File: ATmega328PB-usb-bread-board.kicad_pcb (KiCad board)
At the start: 2 copper layers, 60 x 60 mm, 32 parts, among them J1 Conn_01x17, J2 Conn_01x17, J3 USB_B_Micro, J4 AVR-ISP-6, J5 Grove-I2C-connector, J6 Grove-I2C-connector, J7 Grove-I2C-connector, U1 ATmega328PB-MU, U2 CP2102N-A01-GQFN28, U3 LMV358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

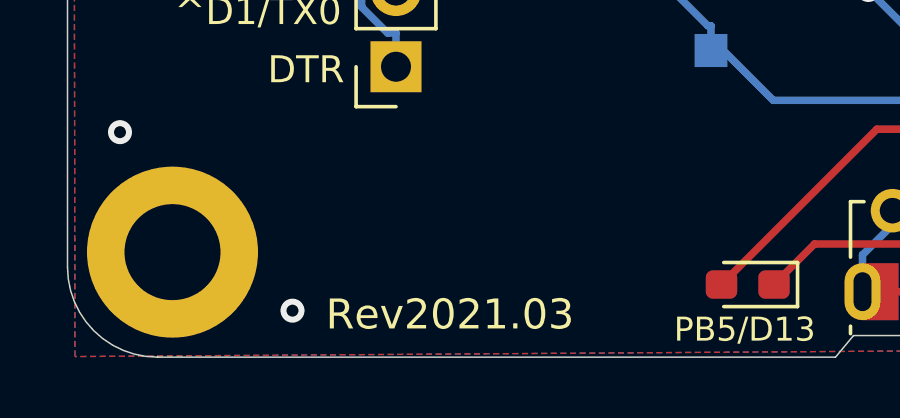
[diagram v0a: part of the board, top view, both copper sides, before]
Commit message: Update revision to Rev2021.04
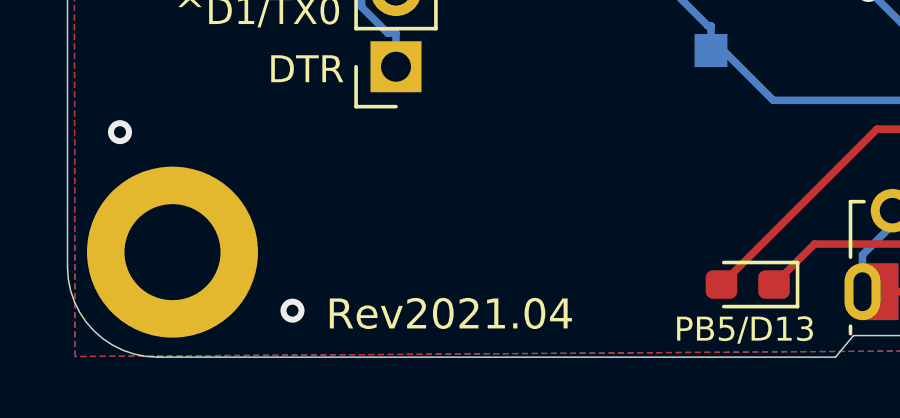
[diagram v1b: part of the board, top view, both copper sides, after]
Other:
- board text added: "Rev2021.04"
- board text removed: "Rev2021.03"
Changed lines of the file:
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@@
     (effects (font (size 1 1) (thickness 0.15)))
   )
-  (gr_text Rev2021.03 (at 112.75 108.58) (layer F.SilkS)
+  (gr_text Rev2021.04 (at 112.75 108.58) (layer F.SilkS)
     (effects (font (size 1 1) (thickness 0.15)))
   )

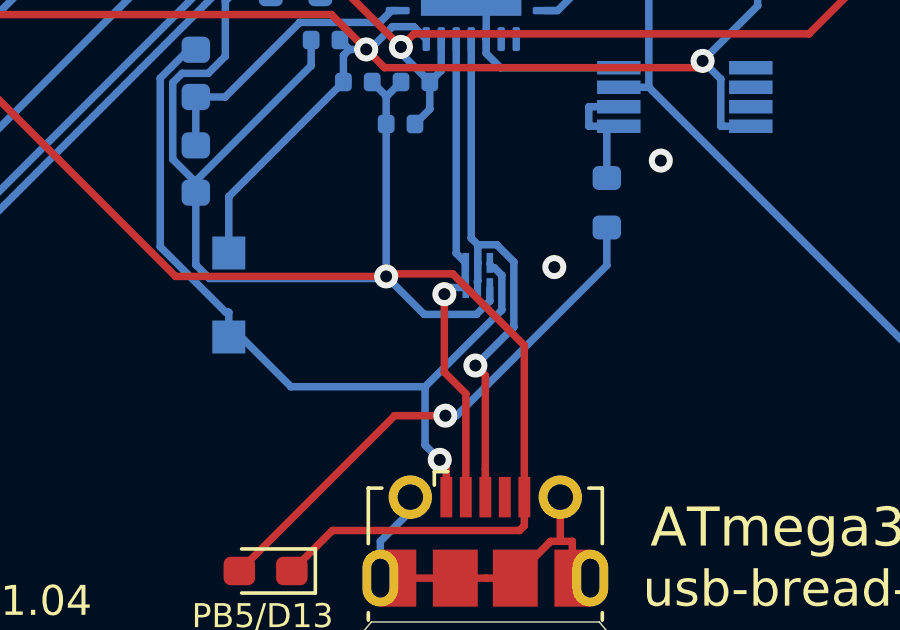
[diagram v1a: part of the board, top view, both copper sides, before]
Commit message: Expand pad for diode array
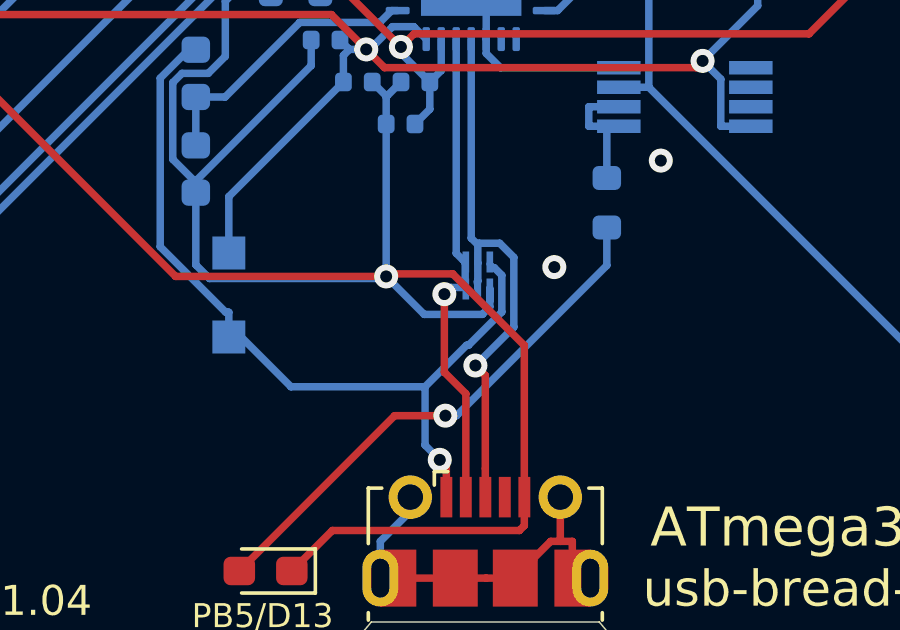
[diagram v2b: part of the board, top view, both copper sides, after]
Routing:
- net GND: track 252.6 -> 253.1 mm

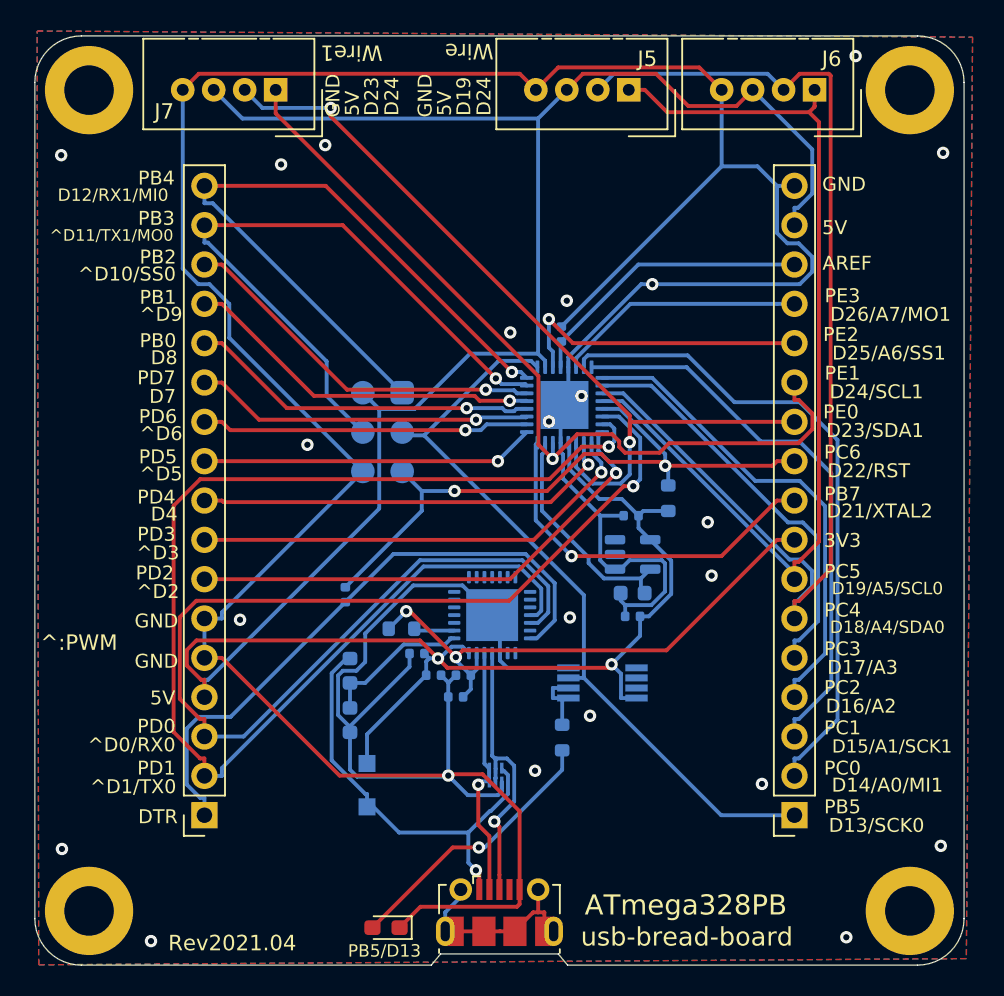
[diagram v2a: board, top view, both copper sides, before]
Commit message: Update footprint position of mems
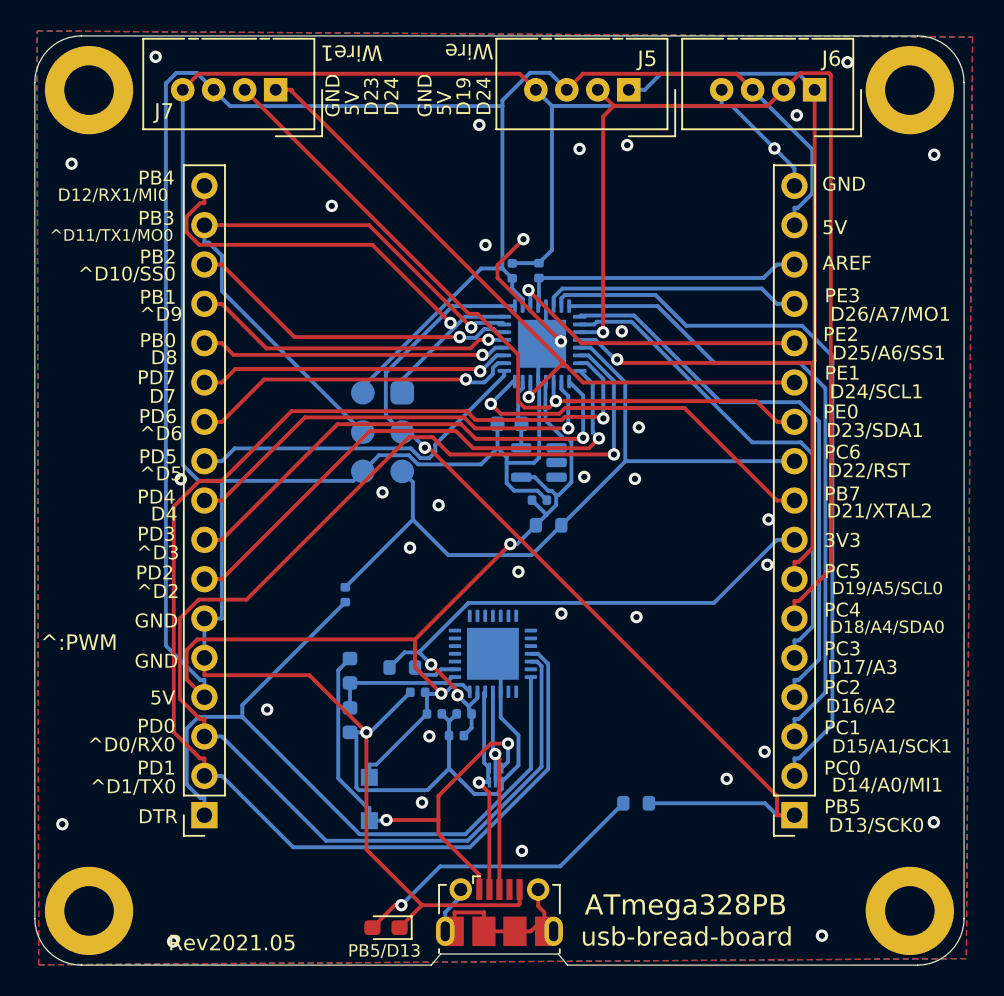
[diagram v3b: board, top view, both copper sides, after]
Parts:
- removed U3: LMV358, Package_SO:VSSOP-8_3.0x3.0mm_P0.65mm
- moved C2 23.6 mm to (130.8, 65.2), turned to 90 degrees
- moved C11 13.5 mm to (130.7, 75.0)
- moved U5 8.48 mm to (132.6, 77.5), turned to 180 degrees
- moved R5 7.92 mm to (133.2, 81.6), turned to 0 degrees
- moved R3 6.39 mm to (138.8, 99.5), turned to 180 degrees
- moved C9 6.00 mm to (132.6, 80.0), turned to 0 degrees
- moved C1 4.35 mm to (132.6, 65.2)
- moved U1 4.21 mm to (132.8, 69.9)
- moved U2 2.50 mm to (129.6, 89.9)
- moved C4 2.50 mm to (124.7, 92.4)
- moved C5 2.50 mm to (125.8, 93.8)
- moved C6 2.50 mm to (127.7, 93.8)
- moved C7 2.50 mm to (127.2, 95.2)
- moved R4 2.50 mm to (123.7, 90.8)
- moved D5 0.91 mm to (121.6, 99.3)
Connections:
- R3 pad 1: Net-(R3-Pad1) -> /pb5
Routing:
- net GND: track 253.1 -> 214.1 mm, vias 23 -> 37
- net /pb4: track 44.9 -> 32.6 mm
- net /pb5: track 49.2 -> 60.4 mm, vias 0 -> 1
- net /16MHz: track 14.8 -> 4.49 mm
- net /DTR: track 39.9 -> 49.7 mm
- net /pe1: track 54.7 -> 45.6 mm
- net /pe0: track 55.4 -> 47.8 mm, vias 2 -> 1
- net VCC: track 171.3 -> 178.7 mm
- net /USB_UART_RX: track 80.8 -> 87.9 mm
- net /pc3: track 26.6 -> 32.5 mm
- net /pc2: track 31.1 -> 36.9 mm
- net /pc1: track 36.5 -> 42.2 mm
- net /pc0: track 42.3 -> 48.0 mm
- net /pc4: track 74.5 -> 69.0 mm, vias 0 -> 1
- net /USB_UART_TX: track 78.4 -> 83.3 mm
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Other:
- board text added: "Rev2021.05"
- board text added: "https://github.com/asukiaaa/ATmega328PB-usb-bread-board"
- board text removed: "Rev2021.04"

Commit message: Update a list of components and update label for resistors
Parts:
- R3: value 10k -> 22k

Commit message: Correct pin label for wire connector
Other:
- board text added: "D18"
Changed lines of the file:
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@@
     (effects (font (size 0.9 0.9) (thickness 0.15)))
   )
-  (gr_text D19 (at 127.7 53.9 90) (layer F.SilkS)
+  (gr_text D18 (at 127.7 53.9 90) (layer F.SilkS)
     (effects (font (size 0.9 0.9) (thickness 0.15)))
   )
-  (gr_text D24 (at 129 53.9 90) (layer F.SilkS)
+  (gr_text D19 (at 129 53.9 90) (layer F.SilkS)
     (effects (font (size 0.9 0.9) (thickness 0.15)))
   )

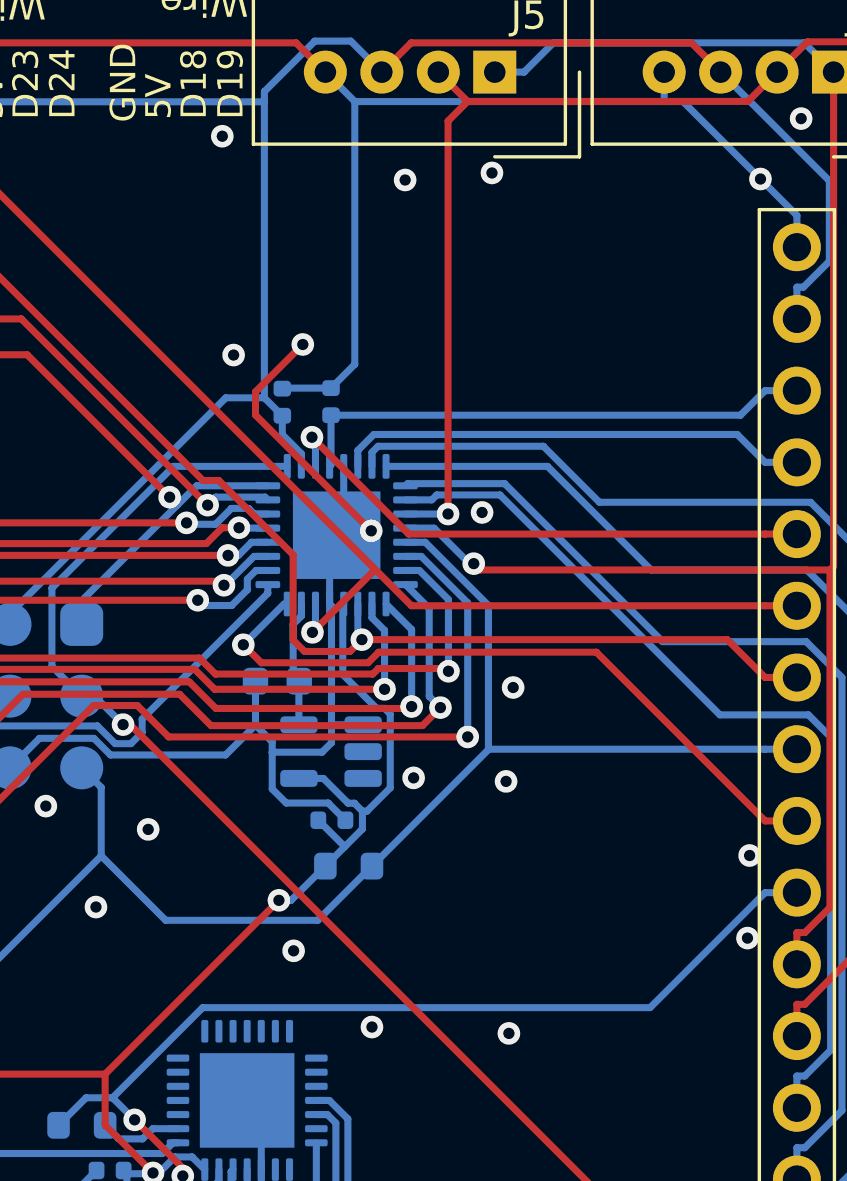
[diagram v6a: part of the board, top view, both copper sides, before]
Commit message: Supply 3V3 for mems
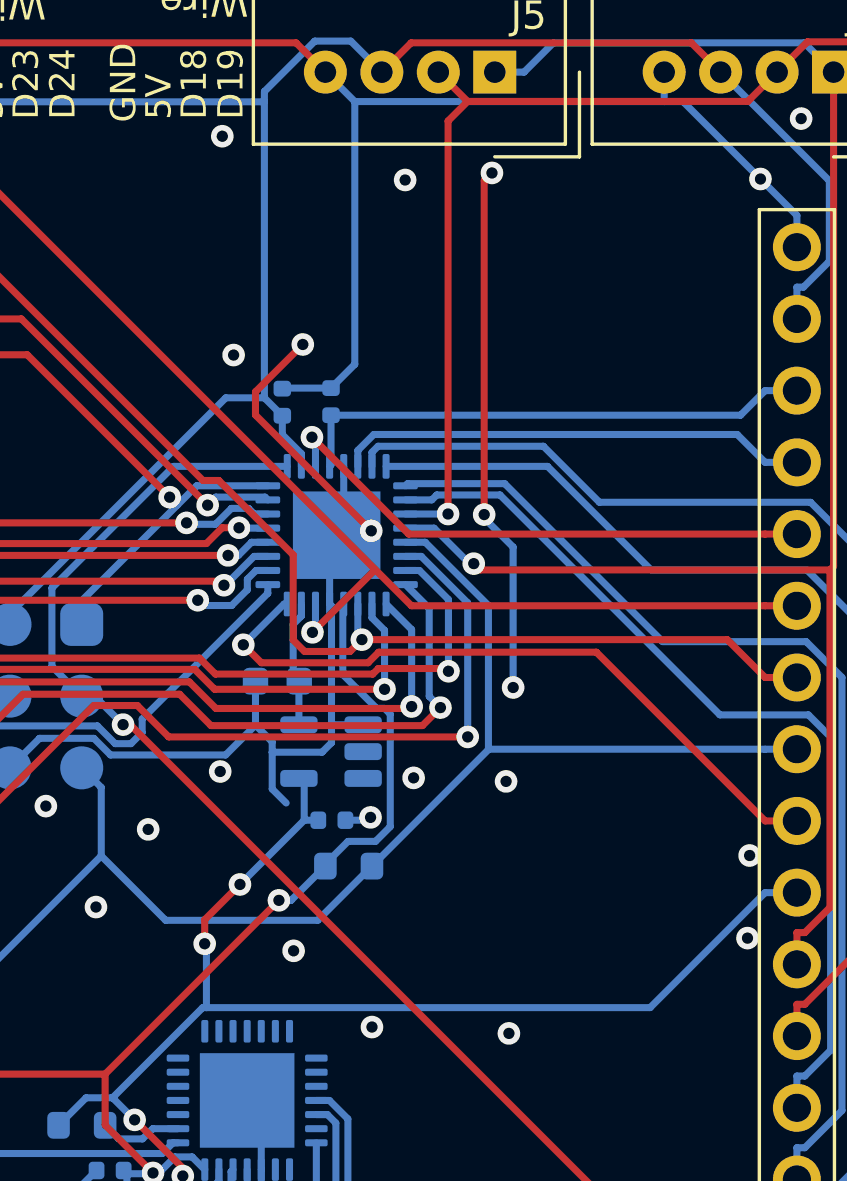
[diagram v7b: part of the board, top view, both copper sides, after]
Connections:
- C9 pad 1: VCC -> +3V3
- U5 pad 4: VCC -> +3V3
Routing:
- net GND: track 214.1 -> 231.4 mm, vias 37 -> 39
- net +3V3: track 37.7 -> 47.9 mm, vias 2 -> 4
- net VCC: track 178.7 -> 175.1 mm

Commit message: Update revision to 2021.06
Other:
- board text added: "Rev2021.06"
- board text removed: "Rev2021.05"
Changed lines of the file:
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@@
     (effects (font (size 1 1) (thickness 0.15)))
   )
-  (gr_text Rev2021.05 (at 112.75 108.58) (layer F.SilkS)
+  (gr_text Rev2021.06 (at 112.75 108.58) (layer F.SilkS)
     (effects (font (size 1 1) (thickness 0.15)))
   )
